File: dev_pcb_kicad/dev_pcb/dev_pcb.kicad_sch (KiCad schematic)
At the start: 1 part, among them U1 XIAO-ESP32-S3-SMD

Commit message: mk1 pcb
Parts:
- removed U1: XIAO-ESP32-S3-SMD, XIAO_Series_Footprints:XIAO-ESP32-S3-SMD, symbol Seeed_Studio_XIAO_Series:XIAO-ESP32-S3-SMD
- added DWM1: DWM3000, RF_Module:DWM1000, symbol RF_Module:DWM3000
- added U2: XIAO-ESP32-S3-DIP, XIAO_Series_Footprints:XIAO-ESP32-S3-DIP, symbol Seeed_Studio_XIAO_Series:XIAO-ESP32-S3-DIP
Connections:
- new net: DWM1.16 (VSS), DWM1.21 (VSS), DWM1.23 (VSS), DWM1.24 (VSS), DWM1.8 (VSS)
- new net: DWM1.17 (~{SPICS}), U2.8 (GPIO44_D7_RX)
- new net: DWM1.18 (SPIMOSI), U2.9 (GPIO7_A8_D8_SCK)
- new net: DWM1.19 (SPIMISO), U2.10 (GPIO8_A9_D9_MISO)
- new net: DWM1.20 (SPICLK), U2.11 (GPIO9_A10_D10_MOSI)
- new net +3.3V: U2.14 (VBUS)

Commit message: .
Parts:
- added D1, D2, D3, D4: LED, LED_SMD:LED_0402_1005Metric_Pad0.77x0.64mm_HandSolder, symbol Device:LED
- added R1: 100K, Resistor_SMD:R_0603_1608Metric_Pad0.98x0.95mm_HandSolder, symbol Device:R
- added R2, R3, R4, R5: 200, Resistor_SMD:R_0805_2012Metric_Pad1.20x1.40mm_HandSolder, symbol Device:R
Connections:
- net +3.3V: now also DWM1.5 (VDDAON), DWM1.6 (VDD3V3), DWM1.7 (VDD3V3), U2.12 (3V3), R2.2, R3.2, R4.2, R5.2; no longer U2.14 (VBUS)
- net at DWM1.1 (EXTON): now also U2.2 (GPIO2_A1_D1)
- net at DWM1.12 (GPIO3/TXLED): now also D4.1 (K)
- net at DWM1.13 (GPIO2/RXLED): now also D3.1 (K)
- net at DWM1.14 (GPIO1/SFDLED): now also D2.1 (K)
- net at DWM1.15 (GPIO0/RXOKLED): now also D1.1 (K)
- net GND: now reaches DWM1.16 (VSS), DWM1.21 (VSS), DWM1.23 (VSS), DWM1.24 (VSS), DWM1.8 (VSS)
- net GND: now also U2.13 (GND), R1.1
- net at DWM1.18 (SPIMOSI): now also U2.11 (GPIO9_A10_D10_MOSI); no longer U2.9 (GPIO7_A8_D8_SCK)
- net at DWM1.2 (WAKEUP): now also U2.3 (GPIO3_A2_D2)
- net at DWM1.20 (SPICLK): now also U2.9 (GPIO7_A8_D8_SCK); no longer U2.11 (GPIO9_A10_D10_MOSI)
- net at DWM1.22 (IRQ/GPIO8): now also U2.1 (GPIO1_A0_D0), R1.2
- net at DWM1.3 (~{RST}): now also U2.4 (GPIO4_A3_D3)
- new net: D1.2 (A), R2.1
- new net: D4.2 (A), R5.1
- new net: D2.2 (A), R3.1
- new net: D3.2 (A), R4.1
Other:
- moved on the sheet: U2

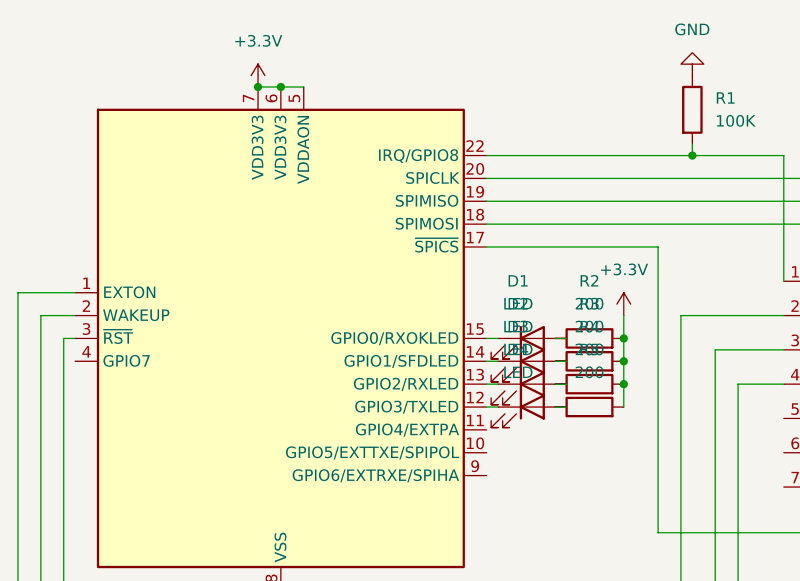
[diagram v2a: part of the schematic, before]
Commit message: small tracing fixes
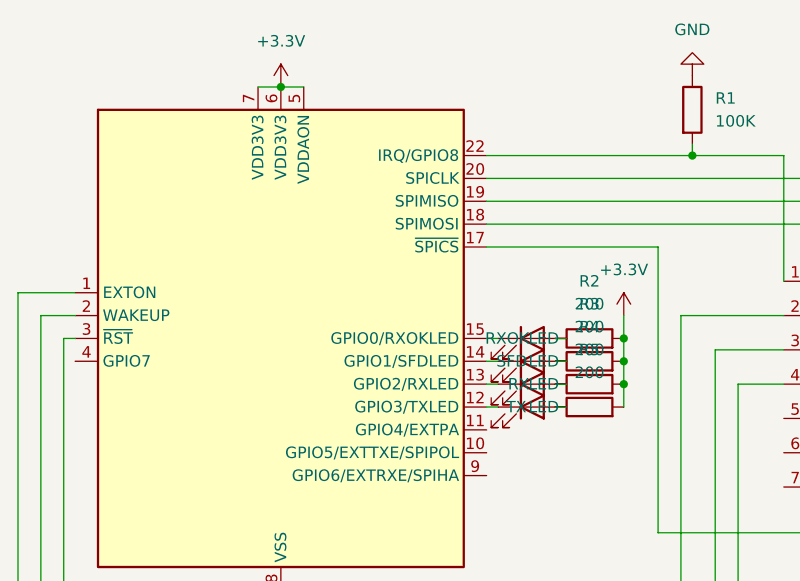
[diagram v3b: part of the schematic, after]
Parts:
- renumbered D3 to RX, D1 to RXOK, D2 to SFD, D4 to TX

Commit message: probe points
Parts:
- added CLK1: CLK, TestPoint:TestPoint_Pad_D1.0mm, symbol Connector:TestPoint_Probe
- added EXTON1, IRQ1, WAKEUP1: TestPoint_Probe, TestPoint:TestPoint_Pad_D1.0mm, symbol Connector:TestPoint_Probe
- added MISO1: MISO, TestPoint:TestPoint_Pad_D1.0mm, symbol Connector:TestPoint_Probe
- added MOSI1: MOSI, TestPoint:TestPoint_Pad_D1.0mm, symbol Connector:TestPoint_Probe
- renumbered RX to RX1, RXOK to RXOK1, SFD to SFD1, TX to TX1
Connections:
- net at DWM1.1 (EXTON), U2.2 (GPIO2_A1_D1): now also EXTON1.1
- net at DWM1.18 (SPIMOSI), U2.11 (GPIO9_A10_D10_MOSI): now also MOSI1.1
- net at DWM1.19 (SPIMISO), U2.10 (GPIO8_A9_D9_MISO): now also CLK1.1
- net at DWM1.2 (WAKEUP), U2.3 (GPIO3_A2_D2): now also WAKEUP1.1
- net at DWM1.20 (SPICLK), U2.9 (GPIO7_A8_D8_SCK): now also MISO1.1
- net at DWM1.22 (IRQ/GPIO8), R1.2, U2.1 (GPIO1_A0_D0): now also IRQ1.1
